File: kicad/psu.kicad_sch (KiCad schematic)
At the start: 22 parts, among them J3 AC Socket, SW4 Power Switch, SW5 120-230, T1 Transformer, U301 LM340T5, U302 AN7805, U303 79L05

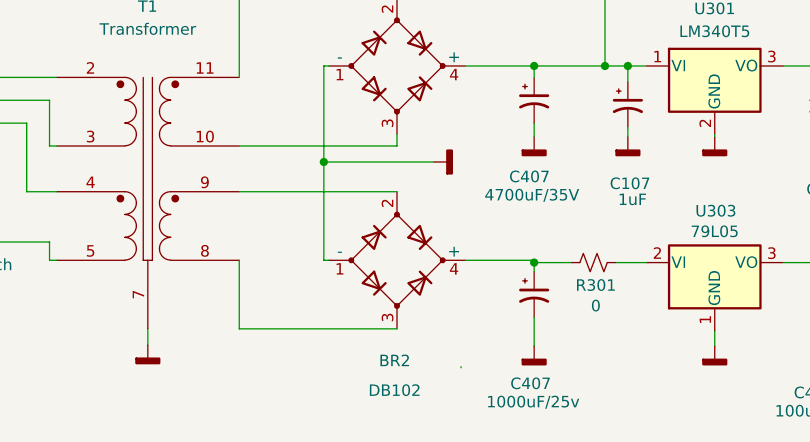
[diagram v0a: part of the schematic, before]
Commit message: Schematic diagram update
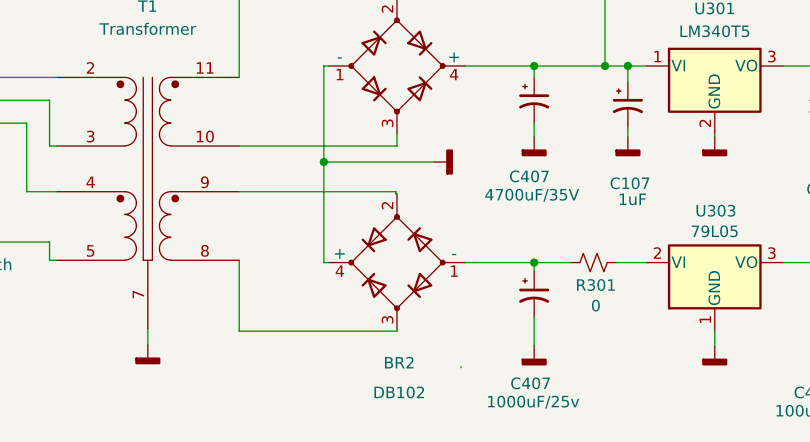
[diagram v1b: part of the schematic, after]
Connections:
- net GNDD: now also BR2.4 (+); no longer BR2.1 (-)
- net at C407.1, R301.1: now also BR2.1 (-); no longer BR2.4 (+)
